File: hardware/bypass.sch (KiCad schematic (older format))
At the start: 1 part

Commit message: Draw bypass circuit
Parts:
- removed K?: RELAY_2RT, symbol RELAY_2RT
- added C? (x2): 100n, symbol C
- added D?: 1N4148, symbol DIODE
- added Q?: BSS138, SOT-23, symbol BSS138
- added R? (x3): 100M, symbol R
- added R?: 10k, symbol R
- added R?: 180, symbol R
- added REL? (x3): Omron G6K-2G-5VCD, symbol Relais_DPDT
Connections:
- net labels added: 9V, Sig-GND
- net labels removed: V+
- wire segments 13 -> 35
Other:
- note removed: "THIS IS A STUB!"

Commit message: Replace Sig-GND label by global GNDA label
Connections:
- net Sig-GND renamed GNDA
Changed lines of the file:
@@
 $Descr A4 11693 8268
 encoding utf-8
-Sheet 6 19
+Sheet 19 19
 Title ""
 Date ""
@@
 Text HLabel 6550 3000 0    60   Input ~ 0
 9V
-Text HLabel 3300 4600 0    60   Input ~ 0
-Sig-GND
 Text HLabel 7200 4150 0    60   Input ~ 0
 Ctrl
@@
 AR Path="/54D120FF/54E8AB86/54D79A29" Ref="REL?"  Part="1"
 AR Path="/54D120FF/54E9BE87/54E9BE9F/54D79A29" Ref="REL?"  Part="1"
+AR Path="/54D120FF/54E9F8A8/54E9BE9F/54D79A29" Ref="REL?"  Part="1"
 F 0 "REL?" H 8050 3500 60  0000 C CNN
 F 1 "Omron G6K-2G-5VCD" H 8050 3600 60  0000 C CNN
@@
 AR Path="/54D120FF/54E8AB86/54D79A79" Ref="REL?"  Part="2"
 AR Path="/54D120FF/54E9BE87/54E9BE9F/54D79A79" Ref="REL?"  Part="2"
+AR Path="/54D120FF/54E9F8A8/54E9BE9F/54D79A79" Ref="REL?"  Part="2"
 F 0 "REL?" H 3700 4000 60  0000 C CNN
 F 1 "Omron G6K-2G-5VCD" H 3700 3500 60  0001 C CNN
@@
 AR Path="/54D120FF/54E8AB86/54D79AAA" Ref="REL?"  Part="3"
 AR Path="/54D120FF/54E9BE87/54E9BE9F/54D79AAA" Ref="REL?"  Part="3"
+AR Path="/54D120FF/54E9F8A8/54E9BE9F/54D79AAA" Ref="REL?"  Part="3"
 F 0 "REL?" H 5200 4000 60  0000 C CNN
 F 1 "Omron G6K-2G-5VCD" H 4850 4150 60  0001 C CNN
@@
 AR Path="/54D120FF/54E8AB86/54D79DA0" Ref="R?"  Part="1"
 AR Path="/54D120FF/54E9BE87/54E9BE9F/54D79DA0" Ref="R?"  Part="1"
+AR Path="/54D120FF/54E9F8A8/54E9BE9F/54D79DA0" Ref="R?"  Part="1"
 F 0 "R?" V 4280 4250 50  0000 C CNN
 F 1 "100M" V 4207 4251 50  0000 C CNN
@@
 AR Path="/54D120FF/54E8AB86/54D79EDE" Ref="R?"  Part="1"
 AR Path="/54D120FF/54E9BE87/54E9BE9F/54D79EDE" Ref="R?"  Part="1"
+AR Path="/54D120FF/54E9F8A8/54E9BE9F/54D79EDE" Ref="R?"  Part="1"
 F 0 "R?" V 4780 4250 50  0000 C CNN
 F 1 "100M" V 4707 4251 50  0000 C CNN
@@
 AR Path="/54D120FF/54E8AB86/54D79F11" Ref="R?"  Part="1"
 AR Path="/54D120FF/54E9BE87/54E9BE9F/54D79F11" Ref="R?"  Part="1"
+AR Path="/54D120FF/54E9F8A8/54E9BE9F/54D79F11" Ref="R?"  Part="1"
 F 0 "R?" V 4530 4250 50  0000 C CNN
 F 1 "100M" V 4457 4251 50  0000 C CNN
@@
 Connection ~ 4450 3900
 Wire Wire Line
-	3300 4600 4200 4600
-Wire Wire Line
 	4200 4600 4450 4600
 Wire Wire Line
-	4450 4600 4700 4600
-Wire Wire Line
 	4700 4600 4700 4500
 Wire Wire Line
 	4450 4500 4450 4600
+Wire Wire Line
+	4450 4600 4450 4700
 Connection ~ 4450 4600
 Wire Wire Line
 	4200 4500 4200 4600
-Connection ~ 4200 4600
 $Comp
 L DIODE D?
@@
 AR Path="/54D120FF/54E8AB86/54D7A6A7" Ref="D?"  Part="1"
 AR Path="/54D120FF/54E9BE87/54E9BE9F/54D7A6A7" Ref="D?"  Part="1"
+AR Path="/54D120FF/54E9F8A8/54E9BE9F/54D7A6A7" Ref="D?"  Part="1"
 F 0 "D?" H 7750 3400 50  0000 C CNN
 F 1 "1N4148" H 7750 3200 50  0000 C CNN
@@
 AR Path="/54D120FF/54E8AB86/54D7A960" Ref="#PWR?"  Part="1"
 AR Path="/54D120FF/54E9BE87/54E9BE9F/54D7A960" Ref="#PWR?"  Part="1"
+AR Path="/54D120FF/54E9F8A8/54E9BE9F/54D7A960" Ref="#PWR?"  Part="1"
 F 0 "#PWR?" H 7900 4500 60  0001 C CNN
 F 1 "GND" H 7900 4600 60  0000 C CNN
@@
 AR Path="/54D120FF/54E8AB86/54D7AAB4" Ref="C?"  Part="1"
 AR Path="/54D120FF/54E9BE87/54E9BE9F/54D7AAB4" Ref="C?"  Part="1"
+AR Path="/54D120FF/54E9F8A8/54E9BE9F/54D7AAB4" Ref="C?"  Part="1"
 F 0 "C?" H 6800 3400 50  0000 L CNN
 F 1 "100n" H 6800 3200 50  0000 L CNN
@@
 AR Path="/54D120FF/54E8AB86/54D7AB88" Ref="#PWR?"  Part="1"
 AR Path="/54D120FF/54E9BE87/54E9BE9F/54D7AB88" Ref="#PWR?"  Part="1"
+AR Path="/54D120FF/54E9F8A8/54E9BE9F/54D7AB88" Ref="#PWR?"  Part="1"
 F 0 "#PWR?" H 6750 3250 60  0001 C CNN
 F 1 "GND" H 6750 3350 60  0000 C CNN
@@
 AR Path="/54D120FF/54E8AB86/54D7ADF3" Ref="R?"  Part="1"
 AR Path="/54D120FF/54E9BE87/54E9BE9F/54D7ADF3" Ref="R?"  Part="1"
+AR Path="/54D120FF/54E9F8A8/54E9BE9F/54D7ADF3" Ref="R?"  Part="1"
 F 0 "R?" V 7580 4500 50  0000 C CNN
 F 1 "10k" V 7507 4501 50  0000 C CNN
@@
 AR Path="/54D120FF/54E8AB86/54D7AECB" Ref="Q?"  Part="1"
 AR Path="/54D120FF/54E9BE87/54E9BE9F/54D7AECB" Ref="Q?"  Part="1"
+AR Path="/54D120FF/54E9F8A8/54E9BE9F/54D7AECB" Ref="Q?"  Part="1"
 F 0 "Q?" H 7800 3951 40  0000 R CNN
 F 1 "BSS138" H 7800 4250 40  0000 R CNN
@@
 AR Path="/54D120FF/54E8AB86/54D7B0C5" Ref="#PWR?"  Part="1"
 AR Path="/54D120FF/54E9BE87/54E9BE9F/54D7B0C5" Ref="#PWR?"  Part="1"
+AR Path="/54D120FF/54E9F8A8/54E9BE9F/54D7B0C5" Ref="#PWR?"  Part="1"
 F 0 "#PWR?" H 7500 4500 60  0001 C CNN
 F 1 "GND" H 7500 4600 60  0000 C CNN
@@
 AR Path="/54D120FF/54E8AB86/54D7C711" Ref="R?"  Part="1"
 AR Path="/54D120FF/54E9BE87/54E9BE9F/54D7C711" Ref="R?"  Part="1"
+AR Path="/54D120FF/54E9F8A8/54E9BE9F/54D7C711" Ref="R?"  Part="1"
 F 0 "R?" V 7180 3000 50  0000 C CNN
 F 1 "180" V 7107 3001 50  0000 C CNN
@@
 AR Path="/54D120FF/54E8AB86/54D7C874" Ref="C?"  Part="1"
 AR Path="/54D120FF/54E9BE87/54E9BE9F/54D7C874" Ref="C?"  Part="1"
+AR Path="/54D120FF/54E9F8A8/54E9BE9F/54D7C874" Ref="C?"  Part="1"
 F 0 "C?" H 7500 3400 50  0000 L CNN
 F 1 "100n" H 7500 3200 50  0000 L CNN
@@
 AR Path="/54D120FF/54E8AB86/54D7C87A" Ref="#PWR?"  Part="1"
 AR Path="/54D120FF/54E9BE87/54E9BE9F/54D7C87A" Ref="#PWR?"  Part="1"
+AR Path="/54D120FF/54E9F8A8/54E9BE9F/54D7C87A" Ref="#PWR?"  Part="1"
 F 0 "#PWR?" H 7450 3250 60  0001 C CNN
 F 1 "GND" H 7450 3350 60  0000 C CNN
@@
 	7450 3100 7450 3000
 Connection ~ 7450 3000
+$Comp
+L GNDA #PWR?
+U 1 1 54EA1C00
+P 4450 4700
+AR Path="/54D120FF/54E9F8A8/54E9BE9F/54EA1C00" Ref="#PWR?"  Part="1"
+AR Path="/54D120FF/54E8FA7B/54EA1C00" Ref="#PWR?"  Part="1"
+AR Path="/54D5349F/54D53732/54EA1C00" Ref="#PWR?"  Part="1"
+F 0 "#PWR?" H 4450 4450 60  0001 C CNN
+F 1 "GNDA" H 4450 4550 60  0000 C CNN
+F 2 "" H 4450 4700 60  0000 C CNN
+F 3 "" H 4450 4700 60  0000 C CNN
+	1    4450 4700
+	1    0    0    -1
+$EndComp
+Wire Wire Line
+	4450 4600 4700 4600
 $EndSCHEMATC

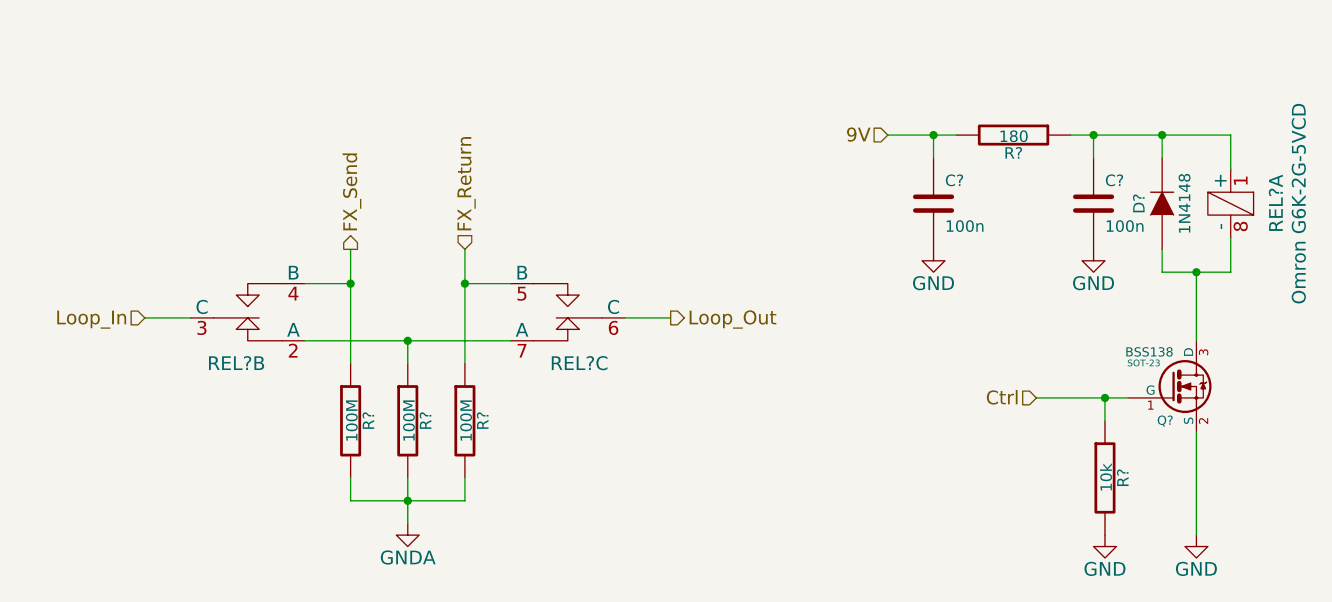
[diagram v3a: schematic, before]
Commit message: Use global label for digital (noisy) 9V
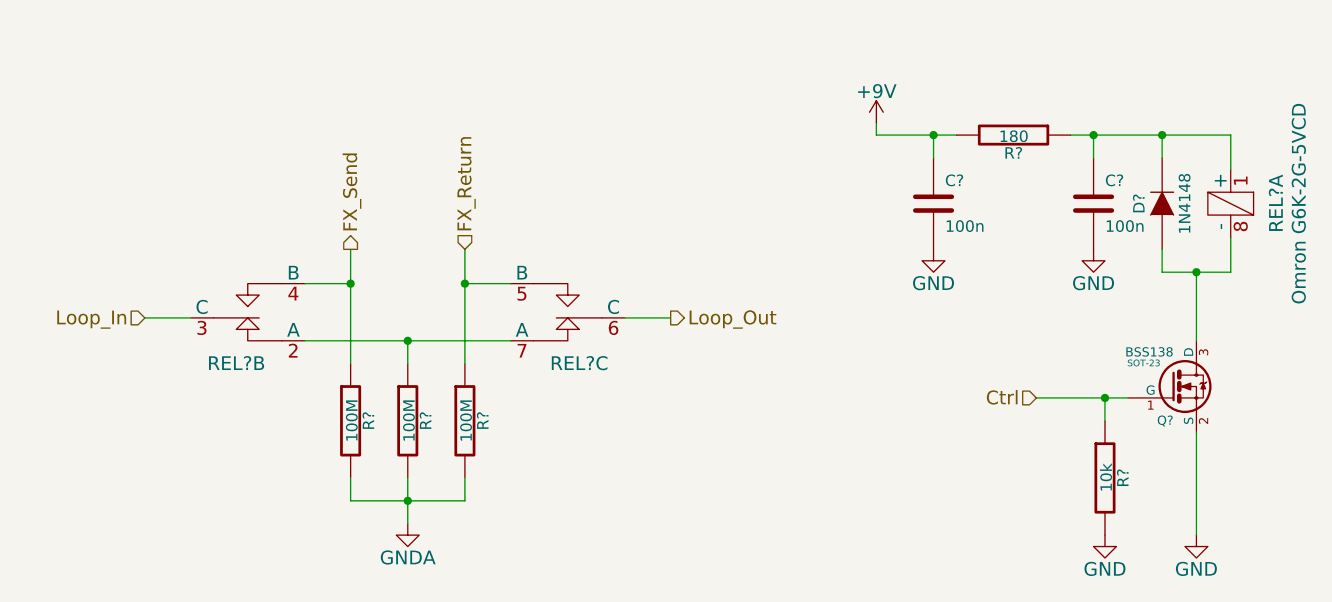
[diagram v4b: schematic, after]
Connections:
- net 9V renamed +9V
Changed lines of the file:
@@
 Text HLabel 4700 3500 1    60   Input ~ 0
 FX_Return
-Text HLabel 6550 3000 0    60   Input ~ 0
-9V
 Text HLabel 7200 4150 0    60   Input ~ 0
 Ctrl
@@
 	3300 3800 3500 3800
 Wire Wire Line
-	4000 3900 4450 3900
-Wire Wire Line
-	4450 3900 4900 3900
+	4000 3900 4900 3900
 Wire Wire Line
 	5400 3800 5600 3800
@@
 	4000 3650 4200 3650
 Wire Wire Line
-	4200 3500 4200 3650
-Wire Wire Line
-	4200 3650 4200 4000
-Wire Wire Line
-	4700 3500 4700 3650
-Wire Wire Line
-	4700 3650 4700 4000
+	4200 3500 4200 4000
+Wire Wire Line
+	4700 3500 4700 4000
 Wire Wire Line
 	4700 3650 4900 3650
@@
 Connection ~ 4450 3900
 Wire Wire Line
-	4200 4600 4450 4600
+	4200 4600 4700 4600
 Wire Wire Line
 	4700 4600 4700 4500
 Wire Wire Line
-	4450 4500 4450 4600
-Wire Wire Line
-	4450 4600 4450 4700
+	4450 4500 4450 4700
 Connection ~ 4450 4600
 Wire Wire Line
@@
 $EndComp
 Wire Wire Line
-	6550 3000 6750 3000
-Wire Wire Line
-	6750 3000 6850 3000
-Wire Wire Line
-	7350 3000 7450 3000
-Wire Wire Line
-	7450 3000 7750 3000
-Wire Wire Line
-	7750 3000 8050 3000
+	6500 3000 6850 3000
+Wire Wire Line
+	7350 3000 8050 3000
 Wire Wire Line
 	7750 3000 7750 3100
@@
 	7750 3500 7750 3600
 Wire Wire Line
-	7750 3600 7900 3600
-Wire Wire Line
-	7900 3600 8050 3600
+	7750 3600 8050 3600
 Wire Wire Line
 	8050 3600 8050 3450
@@
 $EndComp
 Wire Wire Line
-	7200 4150 7500 4150
-Wire Wire Line
-	7500 4150 7600 4150
+	7200 4150 7600 4150
 Wire Wire Line
 	7500 4150 7500 4250
@@
 	1    0    0    -1
 $EndComp
-Wire Wire Line
-	4450 4600 4700 4600
+$Comp
+L +9V #PWR?
+U 1 1 54E940D4
+P 6500 2950
+AR Path="/54D120FF/54E9F8A8/54E9BE9F/54E940D4" Ref="#PWR?"  Part="1"
+AR Path="/54D5349F/54D53732/54E940D4" Ref="#PWR?"  Part="1"
+F 0 "#PWR?" H 6500 2800 60  0001 C CNN
+F 1 "+9V" H 6500 3090 60  0000 C CNN
+F 2 "" H 6500 2950 60  0000 C CNN
+F 3 "" H 6500 2950 60  0000 C CNN
+	1    6500 2950
+	1    0    0    -1
+$EndComp
+Wire Wire Line
+	6500 2950 6500 3000
 $EndSCHEMATC
